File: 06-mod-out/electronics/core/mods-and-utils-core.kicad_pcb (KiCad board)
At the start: 2 copper layers, 58 x 65 mm, 70 parts, among them J2 Conn_02x03_Odd_Even, J3 Conn_02x03_Odd_Even, J4 Conn_02x06_Odd_Even, J5 Conn_02x03_Odd_Even, J6 Conn_01x02, J7 Conn_02x05_Odd_Even, J8 Conn_02x03_Odd_Even, Q1 BC857, Q2 BC847, Q3 BC847BS, U1 LM324, U2 TL072

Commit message: Added double defaults pin row to ADSR
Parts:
- J4: value Conn_02x06_Odd_Even -> Conn_01x06; footprint Connector_PinHeader_2.54mm:PinHeader_2x06_P2.54mm_Vertical -> Connector_PinHeader_2.54mm:PinHeader_1x06_P2.54mm_Vertical
- moved J4 2.50 mm to (143.0, 47.0)
- moved R11 1.30 mm to (149.5, 51.9)
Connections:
- J4 pad 1: Net-(J4-Pin_1) -> unconnected-(J4-Pin_1-Pad1)
- J4 pad 2: Net-(J4-Pin_1) -> unconnected-(J4-Pin_2-Pad2)
- J4 pad 3: Net-(J4-Pin_3) -> unconnected-(J4-Pin_3-Pad3)
- J4 pad 4: Net-(J4-Pin_3) -> unconnected-(J4-Pin_4-Pad4)
- J4 pad 5: Net-(J4-Pin_5) -> unconnected-(J4-Pin_5-Pad5)
- J4 pad 6: Net-(J4-Pin_5) -> unconnected-(J4-Pin_6-Pad6)
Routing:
- net Net-(J4-Pin_7): track 2.54 -> 0.00 mm
- net Net-(J4-Pin_5): track 2.54 -> 0.00 mm
- net Net-(J4-Pin_3): track 2.54 -> 0.00 mm
- net Net-(J4-Pin_11): track 2.54 -> 0.00 mm
- net Net-(J4-Pin_10): track 2.54 -> 0.00 mm
- net Net-(J4-Pin_1): track 2.54 -> 0.00 mm
- net SUSTAIN_3: track 8.04 -> 6.29 mm
- net Net-(D3-A): track 40.4 -> 39.3 mm
- net GND: vias 340 -> 344
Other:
- board text added: "DEFAULTS"

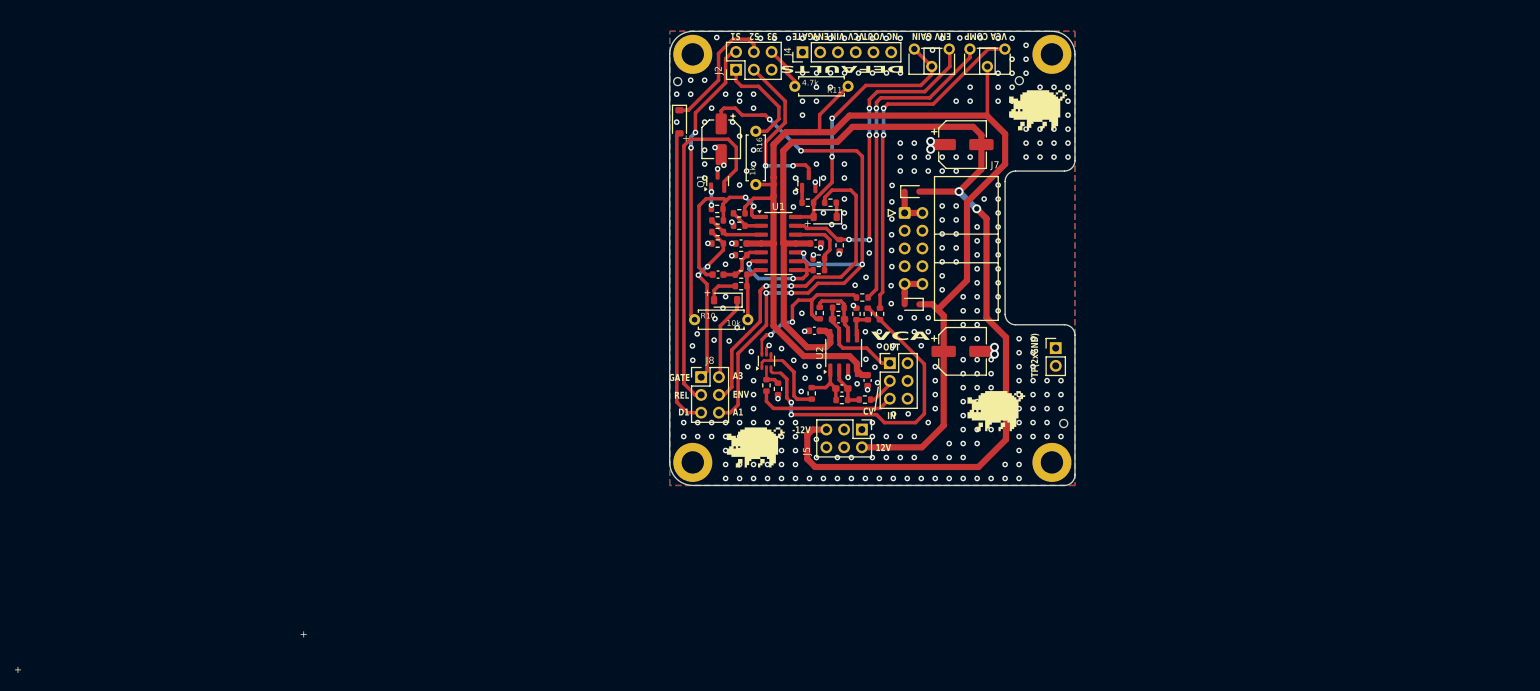
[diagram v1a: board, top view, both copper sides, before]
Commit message: Started Mod/Output PCB
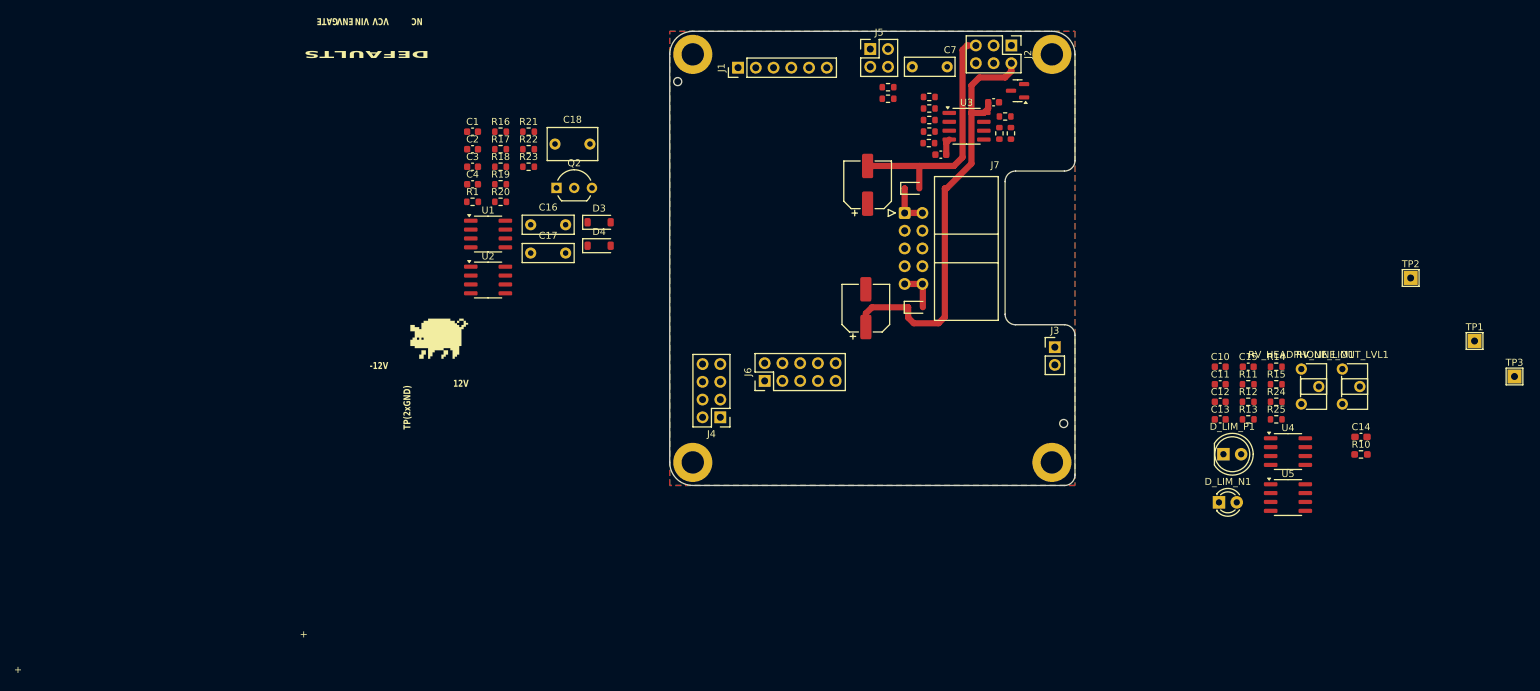
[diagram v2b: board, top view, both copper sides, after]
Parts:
- removed D5: 1N5817, Diode_SMD:D_SOD-323
- removed the G*** at (176.7, 55.3)
- removed the G*** at (170.7, 98.4)
- removed the G*** at (159.4, 54.8)
- removed the G*** at (166.0, 102.3)
- removed J8: Conn_02x03_Odd_Even, Connector_PinHeader_2.54mm:PinHeader_2x03_P2.54mm_Vertical
- removed Q1: BC857, Package_TO_SOT_SMD:SOT-23
- removed Q3: BC847BS, Package_TO_SOT_SMD:SOT-363_SC-70-6
- removed R28: 470k, Resistor_SMD:R_0603_1608Metric
- removed the REF** at (174.0, 51.1)
- removed RV_COMP1: 10k, Potentiometer_THT:Potentiometer_ACP_CA6-H2,5_Horizontal
- removed RV_OUT_GAIN1: 100k, Potentiometer_THT:Potentiometer_ACP_CA6-H2,5_Horizontal
- added C11: 100n, Capacitor_SMD:C_0603_1608Metric, F.Cu at (202.8, 94.5)
- added C12: 100n, Capacitor_SMD:C_0603_1608Metric, F.Cu at (202.8, 97.0)
- added C13: 100n, Capacitor_SMD:C_0603_1608Metric, F.Cu at (202.8, 99.5)
- added C14: 1u, Capacitor_SMD:C_0603_1608Metric_Pad1.08x0.95mm_HandSolder, F.Cu at (222.9, 102.0)
- added C15: 100p, Capacitor_SMD:C_0603_1608Metric, F.Cu at (206.8, 92.0)
- added C16: 100n (foil), Capacitor_THT:C_Rect_L7.2mm_W2.5mm_P5.00mm_FKS2_FKP2_MKS2_MKP2, F.Cu at (104.1, 71.7)
- added C17: 100n (foil), Capacitor_THT:C_Rect_L7.2mm_W2.5mm_P5.00mm_FKS2_FKP2_MKS2_MKP2, F.Cu at (104.1, 75.7)
- added C18: 1u (foil), Capacitor_THT:C_Rect_L7.0mm_W4.5mm_P5.00mm, F.Cu at (107.6, 60.1)
- added D_LIM_N1: Red LED, LED_THT:LED_D3.0mm, F.Cu at (202.6, 111.4)
- added D_LIM_P1: Red LED, LED_THT:LED_D5.0mm, F.Cu at (203.2, 104.5)
- added J1: Conn_01x06, Connector_PinHeader_2.54mm:PinHeader_1x06_P2.54mm_Vertical, F.Cu at (133.8, 49.2)
- added Q4: BC848, Package_TO_SOT_SMD:SOT-23, F.Cu at (173.8, 52.5)
- added RV_HEADPHONE_LIM1: 100k, Potentiometer_THT:Potentiometer_ACP_CA6-H2,5_Horizontal, F.Cu at (214.4, 92.3)
- added RV_LINE_OUT_LVL1: 10k, Potentiometer_THT:Potentiometer_ACP_CA6-H2,5_Horizontal, F.Cu at (220.3, 92.3)
- added TP1: MAX_LINEOUT, TestPoint:TestPoint_THTPad_2.0x2.0mm_Drill1.0mm, F.Cu at (239.2, 88.3)
- added TP2: MAINOUT, TestPoint:TestPoint_THTPad_2.0x2.0mm_Drill1.0mm, F.Cu at (230.0, 79.3)
- added TP3: PHONES_OUT, TestPoint:TestPoint_THTPad_2.0x2.0mm_Drill1.0mm, F.Cu at (244.9, 93.4)
- added U3: TL072, Package_SO:SOIC-8_3.9x4.9mm_P1.27mm, F.Cu at (166.5, 57.6)
- added U4: NE5532, Package_SO:SOIC-8_3.9x4.9mm_P1.27mm, F.Cu at (212.5, 104.2)
- added U5: TL072, Package_SO:SOIC-8_3.9x4.9mm_P1.27mm, F.Cu at (212.5, 110.7)
- C10: value 100u -> 100n; footprint Capacitor_SMD:CP_Elec_6.3x7.7 -> Capacitor_SMD:C_0603_1608Metric
- C3: value 10n -> 100n
- C4: value 10u -> 100n; footprint Capacitor_SMD:CP_Elec_5x5.4 -> Capacitor_SMD:C_0603_1608Metric
- C7: value 47p -> 22n-47n (foil); footprint Capacitor_SMD:C_0603_1608Metric_Pad1.08x0.95mm_HandSolder -> Capacitor_THT:C_Rect_L7.0mm_W2.5mm_P5.00mm
- C8: value 47p -> 100u; footprint Capacitor_SMD:C_0603_1608Metric_Pad1.08x0.95mm_HandSolder -> Capacitor_SMD:CP_Elec_6.3x7.7
- D1, D2: value 1N4148 -> 1N5817; footprint Diode_SMD:D_SOD-123 -> Diode_SMD:D_SOD-323
- D4: value 1N5817 -> 1N4148; footprint Diode_SMD:D_SOD-323 -> Diode_SMD:D_SOD-123
- J3: value Conn_02x03_Odd_Even -> Conn_01x02; footprint Connector_PinHeader_2.54mm:PinHeader_2x03_P2.54mm_Vertical -> Connector_PinHeader_2.54mm:PinHeader_1x02_P2.54mm_Vertical
- J4: value Conn_01x06 -> Conn_02x04_Odd_Even; footprint Connector_PinHeader_2.54mm:PinHeader_1x06_P2.54mm_Vertical -> Connector_PinHeader_2.54mm:PinHeader_2x04_P2.54mm_Vertical
- J5: value Conn_02x03_Odd_Even -> Conn_02x02_Odd_Even; footprint Connector_PinHeader_2.54mm:PinHeader_2x03_P2.54mm_Vertical -> Connector_PinHeader_2.54mm:PinHeader_2x02_P2.54mm_Vertical
- J6: value Conn_01x02 -> Conn_02x05_Odd_Even; footprint Connector_PinHeader_2.54mm:PinHeader_1x02_P2.54mm_Vertical -> Connector_PinHeader_2.54mm:PinHeader_2x05_P2.54mm_Vertical
- Q2: value BC847 -> 2N3819; footprint Package_TO_SOT_SMD:SOT-23 -> Package_TO_SOT_THT:TO-92_Inline_Wide
- R1: value 22k -> 33k
- R10: value 10k -> 100k; footprint Shmoergh_Custom_Footprints:R_Axial_DIN0207_L6.3mm_D2.5mm_P7.62mm_Horizontal -> Resistor_SMD:R_0603_1608Metric_Pad0.98x0.95mm_HandSolder
- R11: footprint Shmoergh_Custom_Footprints:R_Axial_DIN0207_L6.3mm_D2.5mm_P7.62mm_Horizontal -> Resistor_SMD:R_0603_1608Metric
- R12: value 10k -> 150
- R13: value 15k -> 1k
- R14, R15: value 47k -> 100
- R16: value 1k -> 1M; footprint Shmoergh_Custom_Footprints:R_Axial_DIN0207_L6.3mm_D2.5mm_P7.62mm_Horizontal -> Resistor_SMD:R_0603_1608Metric
- R18: value 100k -> 10k
- R19: value 200k -> 100k
- R2, R4: value 1k -> 100k
- R20: value 220 -> 10k
- R21: value 33k -> 100k
- R23: value 10k -> 100k
- R24, R8: value 100k -> 47k
- R25: value 10k -> 1k
- R26: value 10k -> 12k
- R27: value 470k -> 47k
- R3: value 47k -> 100k
- R5, R6: value 1M -> 100k
- R7: value 1M -> 10k
- R9: value 1k -> 47k
- U1: value LM324 -> TL072; footprint Package_SO:SOIC-14_3.9x8.7mm_P1.27mm -> Package_SO:SOIC-8_3.9x4.9mm_P1.27mm
- moved R10 97.3 mm to (222.9, 104.6)
- moved R15 71.9 mm to (210.8, 94.5)
- moved R11 71.4 mm to (206.8, 94.5), turned to 0 degrees
- moved R25 67.1 mm to (210.8, 99.5), turned to 0 degrees
- moved R13 65.6 mm to (206.8, 99.5)
- moved R14 64.9 mm to (210.8, 92.0), turned to 0 degrees
- moved R12 64.3 mm to (206.8, 97.0), turned to 0 degrees
- moved G*** 64.0 mm to (82.2, 57.7)
- moved R19 60.6 mm to (99.8, 65.9), turned to 0 degrees
- moved R21 59.0 mm to (103.8, 58.4), turned to 0 degrees
- moved R24 58.1 mm to (210.8, 97.0), turned to 0 degrees
- moved J5 54.5 mm to (152.7, 46.5), turned to 0 degrees
- moved J4 53.6 mm to (131.2, 99.2), turned to 180 degrees
- moved R22 52.3 mm to (103.8, 60.9)
- moved U2 52.0 mm to (98.0, 79.6), turned to 0 degrees
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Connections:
- C10 pad 1: GND -> +12V
- C10 pad 2: -12V -> GND
- C3 pad 1: Net-(C3-Pad1) -> +12V
- C3 pad 2: Net-(U1B-+) -> GND
- C4 pad 1: A1_D3_R3 -> GND
- C4 pad 2: GND -> -12V
- C7 pad 1: Net-(U2A--) -> LFO_TRI
- C7 pad 2: Net-(C7-Pad2) -> Net-(U3A--)
- C8 pad 1: Net-(U2B--) -> +12V
- C8 pad 2: VCA_OUT -> GND
- C9 pad 1: +12V -> GND
- C9 pad 2: GND -> -12V
- D1 pad 1: ATTACK_3 -> +12V
- D2 pad 1: SUSTAIN_2 -> Net-(D2-K)
- D2 pad 2: DECAY_1 -> -12V
- D4 pad 1: +12V -> Net-(D4-K)
- J2 pad 1: LED_A -> GND
- J2 pad 2: SUSTAIN_1 -> +12V
- J2 pad 3: LED_K -> GND
- J2 pad 4: SUSTAIN_2 -> GND
- J2 pad 5: GND -> -12V
- J2 pad 6: SUSTAIN_3 -> GND
- J3 pad 1: VCA_OUT -> GND
- J4 pad 1: unconnected-(J4-Pin_1-Pad1) -> CRUSH_IN
- J4 pad 2: unconnected-(J4-Pin_2-Pad2) -> CRUSH_OUT
- J4 pad 3: unconnected-(J4-Pin_3-Pad3) -> CRUSH_TRIG
- J4 pad 4: unconnected-(J4-Pin_4-Pad4) -> CRUSH_TRIG_DEFAULT
- J4 pad 5: unconnected-(J4-Pin_5-Pad5) -> RV_CRUSH_1
- J4 pad 6: unconnected-(J4-Pin_6-Pad6) -> RV_CRUSH_3
- J5 pad 1: GND -> LFO_RATE
- J5 pad 2: +12V -> LFO_TRI
- J5 pad 4: GND -> LFO_SQR
- J6 pad 1: GND -> OUTPUT_DRIVE_1
- J6 pad 2: GND -> OUTPUT_VOL_2
- J7 pad 1: Net-(D5-K) -> Net-(D2-K)
- J7 pad 10: Net-(D4-A) -> Net-(D1-A)
- J7 pad 2: Net-(D5-K) -> Net-(D2-K)
- J7 pad 9: Net-(D4-A) -> Net-(D1-A)
- Q2 pad 1: Net-(Q2-B) -> Net-(Q2-D)
- Q2 pad 2: GND -> Net-(D4-A)
- Q2 pad 3: LED_K -> Net-(Q2-S)
- R1 pad 1: Net-(U1A--) -> GND
- R1 pad 2: +12V -> Net-(U2B--)
- R10 pad 1: SUSTAIN_1 -> GND
- R10 pad 2: Net-(R10-Pad2) -> Net-(U5A-+)
- R11 pad 1: +12V -> OUTPUT_LINE_OUT
- R11 pad 2: SUSTAIN_3 -> Net-(U5B--)
- R12 pad 1: Net-(U1D-+) -> OUTPUT_LINE_OUT
- R12 pad 2: Net-(U1B--) -> Net-(R12-Pad2)
- R13 pad 1: GND -> OUTPUT_LINE_OUT
- R13 pad 2: Net-(U1D-+) -> Net-(R13-Pad2)
- R14 pad 1: GND -> OUTPUT_PHONES_OUT
- R14 pad 2: Net-(U1D--) -> Net-(U4B--)
- R15 pad 1: Net-(Q2-B) -> OUTPUT_PHONES_OUT
- R15 pad 2: Net-(D3-A) -> Net-(U4A--)
- R16 pad 1: LED_A -> Net-(D4-A)
- R16 pad 2: +12V -> Net-(Q2-D)
- R17 pad 1: ENV_OUT -> Net-(U1B--)
- R17 pad 2: Net-(D3-K) -> CRUSH_OUT
- R18 pad 1: VCA_IN -> Net-(U2A--)
- R18 pad 2: Net-(Q3A-B1) -> CRUSH_TRIG_DEFAULT
- R19 pad 1: VCA_CV -> RV_CRUSH_3
- R19 pad 2: Net-(U2A--) -> CRUSH_TRIG_DEFAULT
- R2 pad 1: GND -> LFO_RATE
- R2 pad 2: Net-(U1A--) -> Net-(U3A--)
- R20 pad 2: Net-(Q3A-B1) -> RV_CRUSH_1
- R21 pad 1: Net-(U2A--) -> GND
- R21 pad 2: Net-(C7-Pad2) -> Net-(D3-A)
- R22 pad 1: Net-(Q3A-C1) -> Net-(U2B--)
- R22 pad 2: Net-(R22-Pad2) -> +12V
- R23 pad 1: Net-(C7-Pad2) -> GND
- R23 pad 2: Net-(Q3A-E1) -> Net-(D3-K)
- R24 pad 1: Net-(Q3B-C2) -> GND
- R24 pad 2: Net-(R24-Pad2) -> OUTPUT_DRIVE_1
- R25 pad 1: Net-(Q3A-C1) -> Net-(D_LIM_N1-K)
- R25 pad 2: Net-(U2B--) -> OUTPUT_DRIVE_3
- R26 pad 1: Net-(Q3B-C2) -> Net-(R26-Pad1)
- R26 pad 2: Net-(U2B-+) -> LFO_SQR
- R27 pad 1: GND -> LFO_SQR
- R27 pad 2: Net-(U2B-+) -> GND
- R3 pad 1: GND -> Net-(U3A-+)
- R3 pad 2: GATE -> LFO_RATE
- R4 pad 1: Net-(U1A-+) -> Net-(Q4-C)
- R4 pad 2: GATE -> Net-(U3A--)
- R5 pad 1: Net-(C3-Pad1) -> Net-(U3A--)
- R5 pad 2: Net-(U1A-+) -> Net-(Q4-C)
- R6 pad 1: GND -> Net-(U3A-+)
- R6 pad 2: Net-(U1B-+) -> GND
- R7 pad 1: Net-(R10-Pad2) -> Net-(R26-Pad1)
- R7 pad 2: Net-(U1B-+) -> Net-(Q4-B)
- R8 pad 1: Net-(Q1-B) -> Net-(U3B-+)
- R8 pad 2: Net-(C3-Pad1) -> GND
- R9 pad 1: Net-(D1-A) -> Net-(U3B-+)
- R9 pad 2: Net-(R10-Pad2) -> Net-(R26-Pad1)
- U1 pad 1: Net-(C3-Pad1) -> Net-(Q2-D)
- U1 pad 2: Net-(U1A--) -> Net-(Q2-D)
- U1 pad 3: Net-(U1A-+) -> CRUSH_IN
- U1 pad 4: +12V -> -12V
- U1 pad 5: Net-(U1B-+) -> Net-(Q2-S)
- U1 pad 7: Net-(R10-Pad2) -> Net-(U1B--)
- U1 pad 8: Net-(U1B--) -> +12V
- U2 pad 1: Net-(C7-Pad2) -> CRUSH_TRIG_DEFAULT
- U2 pad 3: GND -> RV_CRUSH_2
- U2 pad 4: +12V -> -12V
- U2 pad 5: Net-(U2B-+) -> Net-(D3-K)
- U2 pad 7: VCA_OUT -> Net-(D4-K)
- U2 pad 8: -12V -> +12V
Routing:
- net -12V: track 160.4 -> 37.2 mm, vias 2 -> 0
- net +12V: track 168.1 -> 61.9 mm
- net A1_D3_R3: track 87.8 -> 0.00 mm, vias 6 -> 0
- net RELEASE_1: track 52.0 -> 0.00 mm
- net Net-(R24-Pad2): track 49.7 -> 0.00 mm, vias 2 -> 0
- net ENV_OUT: track 48.7 -> 0.00 mm, vias 2 -> 0
- net Net-(U1D--): track 47.5 -> 0.00 mm, vias 4 -> 0
- net Net-(Q3B-C2): track 47.2 -> 0.00 mm, vias 2 -> 0
- net Net-(R22-Pad2): track 45.7 -> 0.00 mm, vias 2 -> 0
- net DECAY_1: track 42.7 -> 0.00 mm
- net SUSTAIN_1: track 41.5 -> 0.00 mm, vias 2 -> 0
- net Net-(D3-A): track 39.3 -> 0.00 mm, vias 2 -> 0
- net Net-(C3-Pad1): track 27.0 -> 0.00 mm, vias 2 -> 0
- net LED_K: track 24.2 -> 0.00 mm, vias 2 -> 0
- net GATE: track 23.9 -> 0.00 mm, vias 2 -> 0
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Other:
- board text removed: "A1"
- board text removed: "A3"
- board text removed: "CV"
- board text removed: "D1"
- board text removed: "IN"
- board text removed: "OUT"
- board text removed: "REL"
- board text removed: "S1"
- board text removed: "S2"
- board text removed: "S3"
- board text removed: "VCA"

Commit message: Designed LFO & Bitcrush PCB
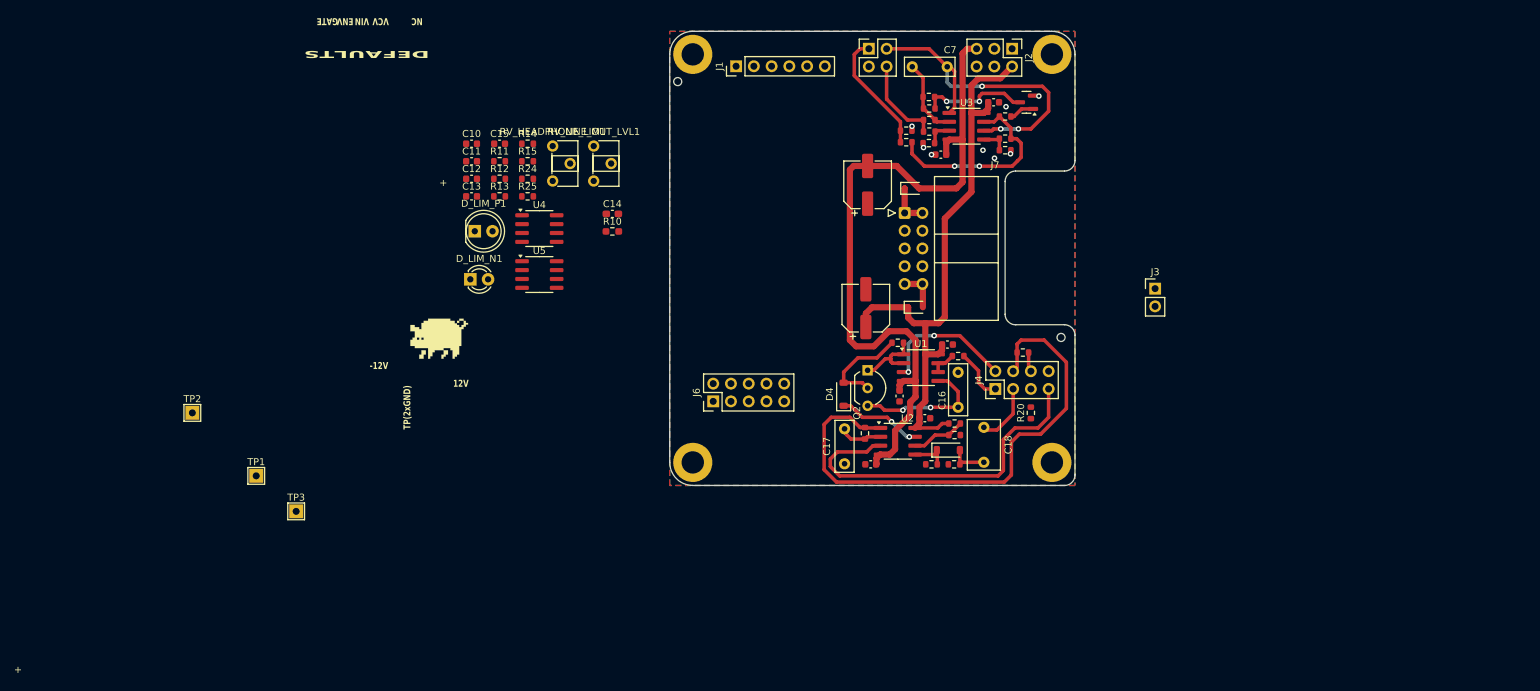
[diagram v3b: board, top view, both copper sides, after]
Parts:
- moved TP1 175.4 mm to (64.8, 107.6)
- moved TP2 175.4 mm to (55.7, 98.6)
- moved TP3 175.4 mm to (70.5, 112.7)
- moved C14 111.8 mm to (115.8, 70.1)
- moved D_LIM_N1 111.8 mm to (95.5, 79.5)
- moved D_LIM_P1 111.8 mm to (96.1, 72.6)
- moved R10 111.8 mm to (115.8, 72.6)
- moved R14 111.8 mm to (103.7, 60.1)
- moved R15 111.8 mm to (103.7, 62.6)
- moved R24 111.8 mm to (103.7, 65.1)
- moved R25 111.8 mm to (103.7, 67.6)
- moved C10 111.8 mm to (95.6, 60.1)
- moved C11 111.8 mm to (95.6, 62.6)
- moved C12 111.8 mm to (95.6, 65.1)
- moved C13 111.8 mm to (95.6, 67.6)
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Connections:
- J4 pad 1: CRUSH_IN -> CRUSH_OUT
- J4 pad 2: CRUSH_OUT -> CRUSH_IN
- J5 pad 1: LFO_RATE -> LFO_SQR
- J5 pad 4: LFO_SQR -> LFO_RATE
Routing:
- net CRUSH_TRIG_DEFAULT: track 0.00 -> 77.4 mm
- net -12V: track 37.2 -> 102.8 mm
- net RV_CRUSH_2: track 0.00 -> 51.0 mm
- net LFO_TRI: track 0.00 -> 47.8 mm, vias 0 -> 3
- net Net-(R26-Pad1): track 0.00 -> 28.7 mm, vias 0 -> 2
- net +12V: track 61.9 -> 85.2 mm
- net Net-(Q2-S): track 0.00 -> 19.1 mm, vias 0 -> 2
- net CRUSH_IN: track 0.00 -> 19.1 mm, vias 0 -> 2
- net LFO_SQR: track 0.00 -> 17.7 mm
- net Net-(Q4-C): track 0.00 -> 15.6 mm, vias 0 -> 2
- net Net-(D4-A): track 0.00 -> 13.9 mm
- net LFO_RATE: track 0.00 -> 12.8 mm
- net Net-(D4-K): track 0.00 -> 11.2 mm, vias 0 -> 2
- net Net-(U3A--): track 0.00 -> 11.2 mm
- net Net-(Q2-D): track 0.00 -> 10.3 mm
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
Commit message: 1st stab at Mod/Output PCB design
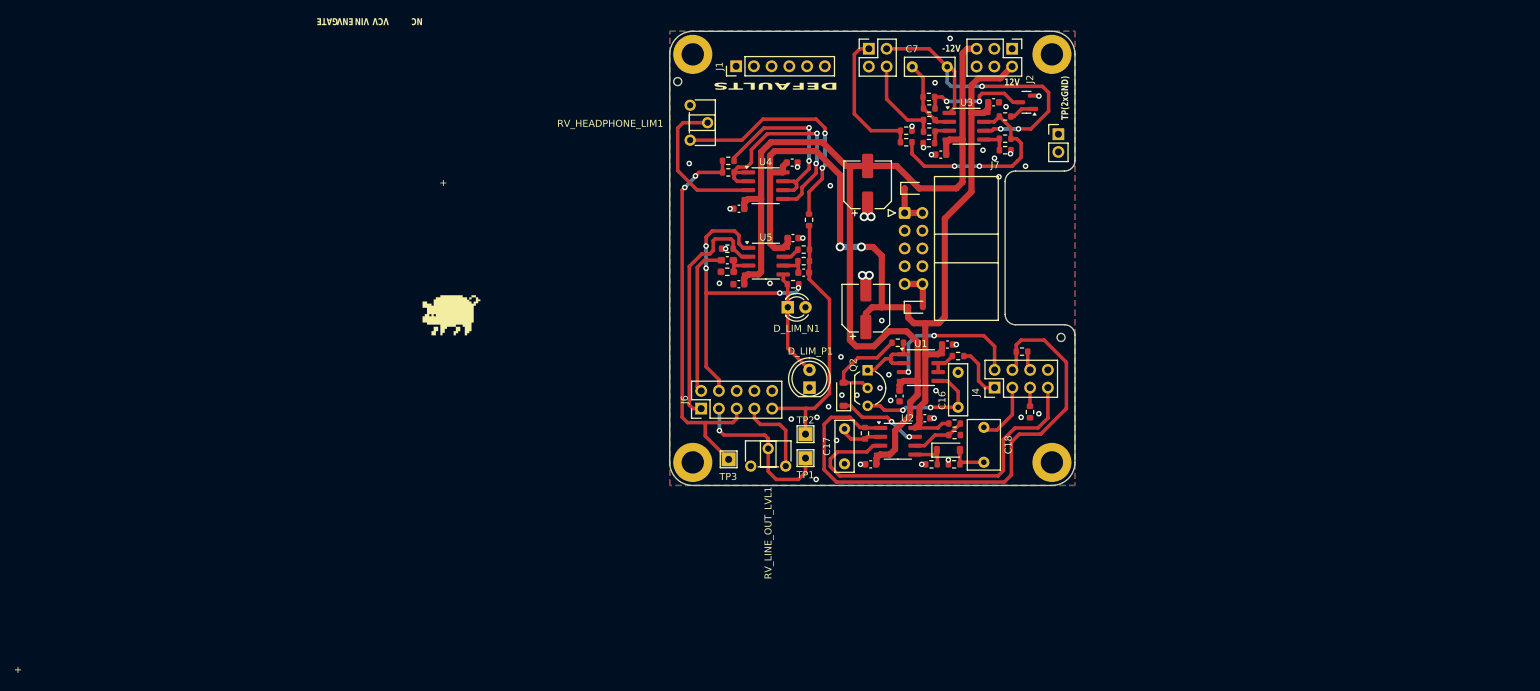
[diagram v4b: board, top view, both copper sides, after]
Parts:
- moved TP2 87.8 mm to (143.4, 101.7)
- moved TP1 78.7 mm to (143.4, 105.1)
- moved TP3 62.3 mm to (132.4, 105.3)
- moved D_LIM_P1 52.9 mm to (144.0, 95.0), turned to 90 degrees
- moved RV_LINE_OUT_LVL1 51.0 mm to (135.6, 106.2), turned to 90 degrees
- moved C10 47.9 mm to (141.6, 73.6)
- moved C15 47.3 mm to (143.2, 78.5)
- moved C12 45.9 mm to (141.5, 62.8)
- moved R11 45.8 mm to (143.2, 76.9), turned to 180 degrees
- moved D_LIM_N1 45.6 mm to (140.9, 83.5)
- moved R12 44.7 mm to (143.2, 75.2), turned to 180 degrees
- moved R13 44.4 mm to (143.9, 71.0), turned to 90 degrees
- moved C11 42.1 mm to (133.9, 80.2)
- moved R25 40.0 mm to (141.7, 80.2)
- moved C13 38.3 mm to (133.9, 69.4)
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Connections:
- J6 pad 3: OUTPUT_DRIVE_3 -> OUTPUT_VOL_3
- J6 pad 4: OUTPUT_VOL_3 -> OUTPUT_DRIVE_3
- J6 pad 7: OUTPUT_LINE_OUT -> OUTPUT_IN
- J6 pad 9: OUTPUT_IN -> OUTPUT_LINE_OUT
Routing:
- net OUTPUT_PHONES_OUT: track 0.00 -> 57.5 mm, vias 0 -> 2
- net +12V: track 85.2 -> 140.9 mm, vias 0 -> 2
- net OUTPUT_DRIVE_3: track 0.00 -> 44.6 mm, vias 0 -> 4
- net -12V: track 102.8 -> 142.8 mm
- net OUTPUT_LINE_OUT: track 0.00 -> 38.1 mm
- net OUTPUT_DRIVE_1: track 0.00 -> 34.4 mm
- net Net-(R13-Pad2): track 0.00 -> 34.3 mm, vias 0 -> 2
- net Net-(U4A--): track 0.00 -> 33.0 mm, vias 0 -> 2
- net Net-(U4B--): track 0.00 -> 26.4 mm, vias 0 -> 2
- net OUTPUT_VOL_3: track 0.00 -> 23.6 mm, vias 0 -> 1
- net Net-(U4A-+): track 0.00 -> 21.9 mm
- net OUTPUT_VOL_2: track 0.00 -> 21.8 mm
- net Net-(D_LIM_N1-K): track 0.00 -> 15.2 mm
- net OUTPUT_IN: track 0.00 -> 11.7 mm
- net Net-(U5B--): track 0.00 -> 3.83 mm
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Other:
- outline, holes or cut-outs redrawn
